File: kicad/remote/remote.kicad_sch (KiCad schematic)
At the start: 14 parts, among them Y1 Resonator

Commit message: KiCAD project: final design for remote
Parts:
- ANT1: DigiKey part # (none) -> 478-M620720TR-ND; MF (none) -> KYOCERA AVX; MP (none) -> M620720
- B1, B2: footprint lock_project:B3F-1000 -> lock_project:SW_PTS645SK43SMTR92LFS; symbol B3F-1000:B3F-1000 -> PTS645SK43SMTR92LFS:PTS645SK43SMTR92LFS; DigiKey part # (none) -> SW400-ND; MANUFACTURER Omron -> CnK; MAXIMUM_PACKAGE_HEIGHT (none) -> 4.4 mm; MF (none) -> CnK; MP (none) -> PTS645SK43SMTR92 LFS; PARTREV (none) -> 14 Apr 22; STANDARD (none) -> Manufacturer Recommendations
- B3: renamed from S1; AVAILABILITY Unavailable -> (none); DESCRIPTION Tactile Switch SPST-NO Top Actuated Surface Mount -> (none); DigiKey part # (none) -> SW1020TR-ND; PACKAGE None -> (none)
- BAT1: value Battery_Cell -> CR2032; DigiKey part # (none) -> BK-912-ND; MF (none) -> MPD (Memory Protection Devices); MP (none) -> BK-912-ND
- C1, C2, R1: PACKAGE (none) -> 0603
- C3, C4: PACKAGE (none) -> 0805
- CPU1: DigiKey part # (none) -> ATMEGA328P-AURTR-ND; MF (none) -> Microchip; MP (none) -> ATMEGA328P-AUR
- ISP1: now not fitted
- RADIO1: renamed from Radio1; MF (none) -> Hoperf; MP (none) -> RFM69HCW
- Y1: value Resonator -> 8MHz; footprint Crystal:Resonator_SMD-3Pin_7.2x3.0mm -> lock_project:CSTNE8M00G550000R0; symbol Device:Resonator -> CSTNE8M00G550000R0:CSTNE8M00G550000R0; Availability (none) -> In Stock; Description_1 (none) -> 8 MHz Ceramic Resonator Built in Capacitor 33 pF ±0.2% 40 O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; MF (none) -> Murata Electronics; MP (none) -> CSTNE8M00G550000R0; Package (none) -> SMD-3 Murata; Price (none) -> None; Purchase-URL (none) -> https://pricing.snapeda.com/search/part/CSTNE8M00G550000R0/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
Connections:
- net GND: now also B1.4, B2.4; no longer B1.1, B2.1
- net PD5: now also B1.2; no longer B1.3
- net PD6: now also B2.2; no longer B2.3

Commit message: Revisted remote board design
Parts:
- added D1: LED, LED_SMD:LED_0603_1608Metric, symbol Device:LED
- added R2: 4.7k, Resistor_SMD:R_0603_1608Metric, symbol Device:R_US
- ANT1: value M620720 -> ~
- BAT1: footprint lock_project:Polycase_BATT-HDR-FB -> lock_project:BAT_BK-912; symbol Device:Battery_Cell -> BK-912:BK-912; MANUFACTURER (none) -> MPD; MAXIMUM_PACKAGE_HEIGHT (none) -> 4.32mm; STANDARD (none) -> Manufacturer recommendations
- C1, C2: footprint Capacitor_SMD:C_0201_0603Metric -> Capacitor_SMD:C_0805_2012Metric
- R1: value 10kOhm -> 10k; footprint Resistor_SMD:R_0201_0603Metric -> Resistor_SMD:R_0603_1608Metric; symbol Device:R -> Device:R_US
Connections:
- net +3.3V: now also BAT1.S1, BAT1.S2, R1.1; no longer BAT1.1 (+), ISP1.2 (VCC), R1.2
- net GND: now also BAT1.1, D1.1 (K); no longer BAT1.2 (-)
- net RESET: now also R1.2; no longer R1.1
- net PC2: now reaches CPU1.25 (PC2)
- net PC2: now also R2.2
- new net: D1.2 (A), R2.1

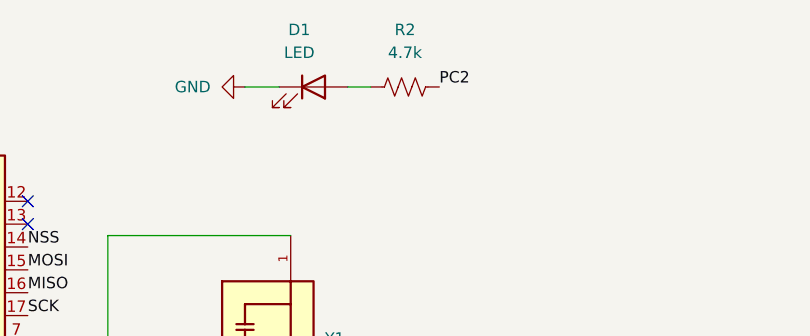
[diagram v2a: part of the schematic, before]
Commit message: kicad: Fix resistor value on remote
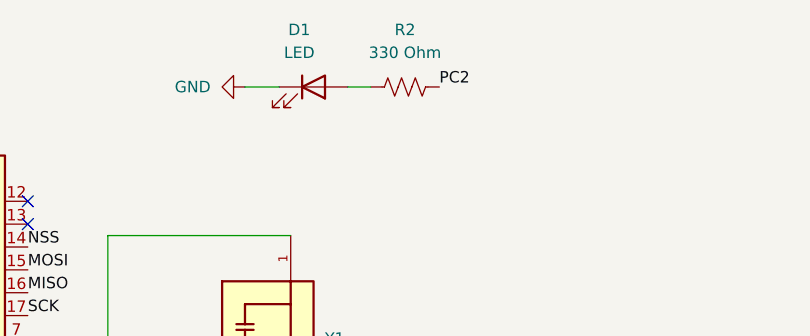
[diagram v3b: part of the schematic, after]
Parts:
- R2: value 4.7k -> 330 Ohm
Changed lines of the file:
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@@
 			)
 		)
-		(property "Value" "4.7k"
+		(property "Value" "330 Ohm"
 			(at 179.07 21.59 90)
 			(effects
